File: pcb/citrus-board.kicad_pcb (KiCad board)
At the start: 4 copper layers, 27 x 60 mm, 65 parts, among them J1 SHOU_HAN_USB_C_Receptacle_USB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, J2 Conn_01x02, J3 Conn_01x03_MountingPin, J4 0.5mm FPC, J5 Conn_01x13, J6 Conn_01x13, SW1 SW_Push, SW2 SW_Push, U1 BQ24074RGT, U2 TPS63000-Q1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

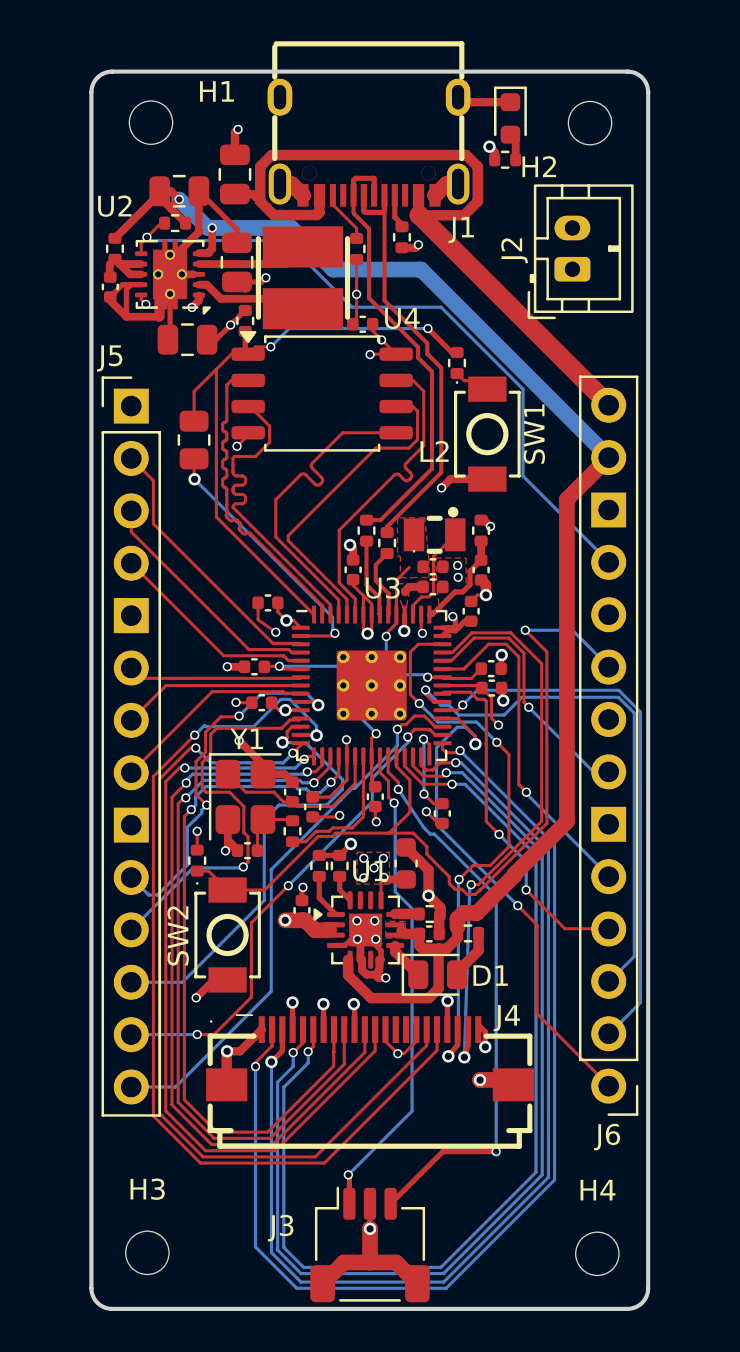
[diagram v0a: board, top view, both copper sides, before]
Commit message: castellated holes + better silkscreen + new images
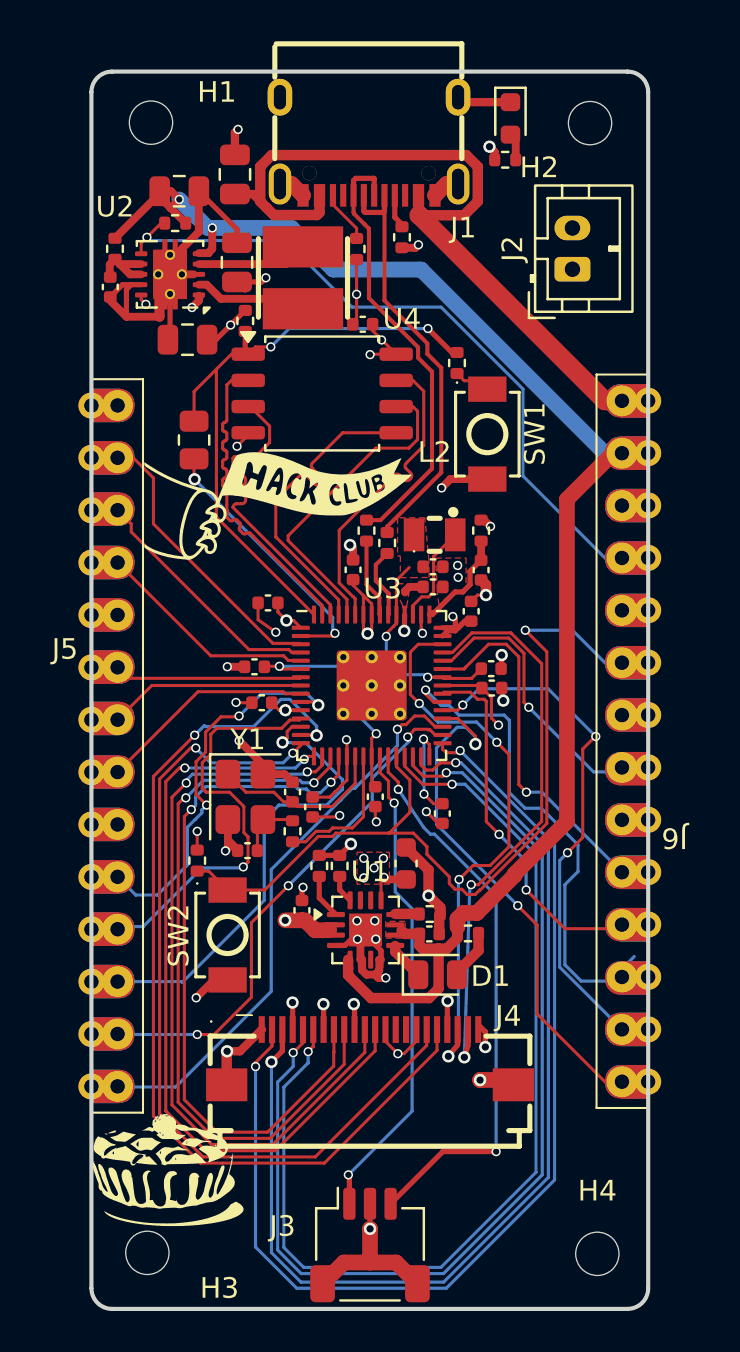
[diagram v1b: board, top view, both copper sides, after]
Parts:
- added G***: LOGO, LOGO, F.Cu at (138.6, 66.0)
- added G***: LOGO, LOGO, F.Cu at (133.0, 98.2)
- added G***: LOGO, LOGO, B.Cu at (138.5, 64.5)
- J5, J6: footprint Connector_PinHeader_2.54mm:PinHeader_1x14_P2.54mm_Vertical -> citrus-lib:Conn_01x14_Castellated
- moved J6 16.7 mm to (155.3, 77.5)
- moved J5 16.5 mm to (130.8, 77.7)
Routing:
- net /GPIO23: track 26.7 -> 25.2 mm, vias 1 -> 3
- net /GPIO24: track 26.0 -> 24.7 mm
- net /GPIO1: track 13.2 -> 13.9 mm
- net /GPIO20: track 24.6 -> 25.2 mm
- net /GPIO3: track 10.2 -> 10.9 mm
- net /GPIO4: track 8.45 -> 9.13 mm
- net /GPIO21: track 26.7 -> 27.4 mm
- net /GPIO9: track 22.0 -> 22.6 mm
- net /GPIO5: track 8.92 -> 9.57 mm
- net /GPIO6: track 9.89 -> 10.5 mm
- net /GPIO8: track 19.7 -> 20.3 mm
- net /GPIO26: track 16.9 -> 17.5 mm
- net VBUS: track 70.6 -> 71.1 mm
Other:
- board text added: "REV.2 21-06-2026 03:54 UTC+10"
- board text added: "its an rpie if u couldn't tell"
- board text removed: "REV.1 21-06-2026 05:54 UTC+10"

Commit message: fix drc and better readme
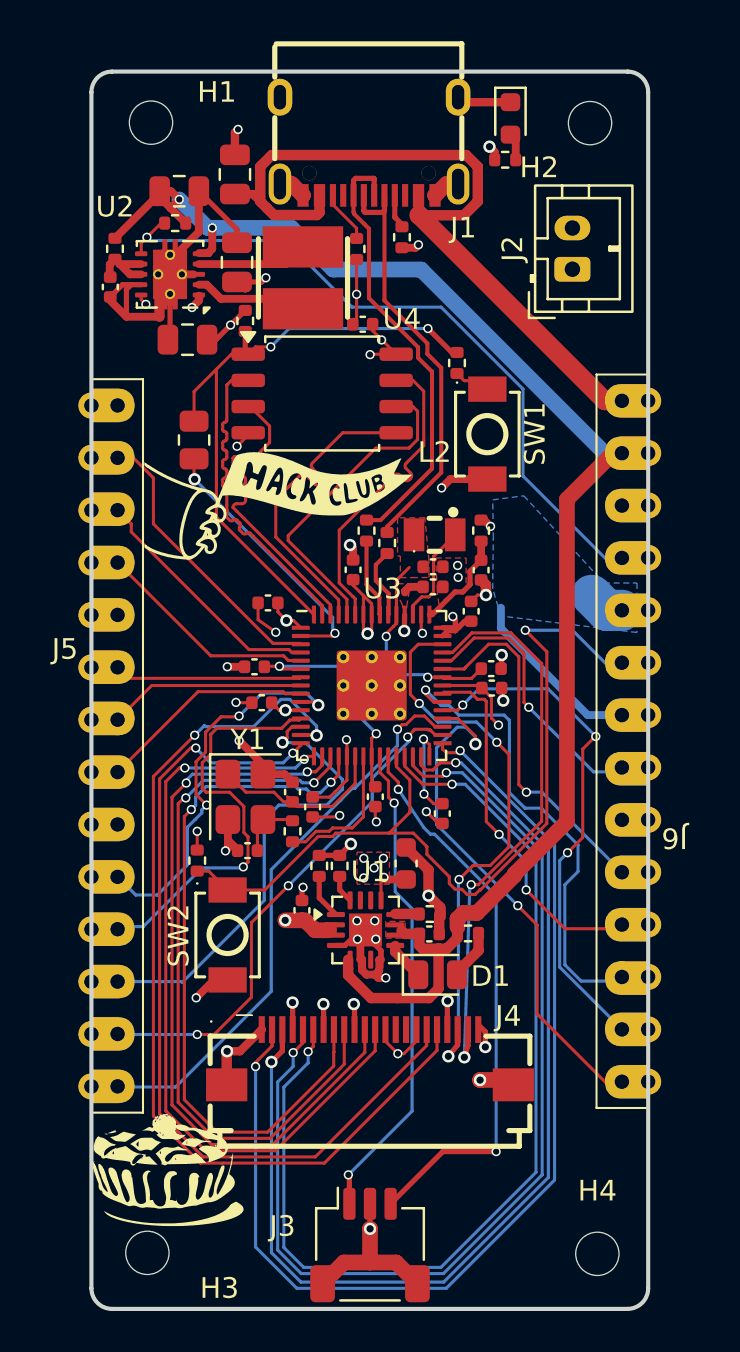
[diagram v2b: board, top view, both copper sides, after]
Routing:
- net +3V3: track 39.4 -> 49.8 mm
- net /GPIO24: track 24.7 -> 23.0 mm
- net VBUS: track 71.1 -> 72.1 mm
- added copper zone on B.Cu, net +3V3
